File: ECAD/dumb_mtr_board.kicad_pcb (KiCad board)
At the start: 4 copper layers, 74.9 x 59.7 mm, 55 parts, among them J1 +5/24V, J2 UART, Q1 SOT-23-3, SW1 REV_BTN, SW2 FWD_BTN, U1 TPS62933DRLR, U2 TMC2209_SILENTSTEPSTICK, U3 LMC555xM

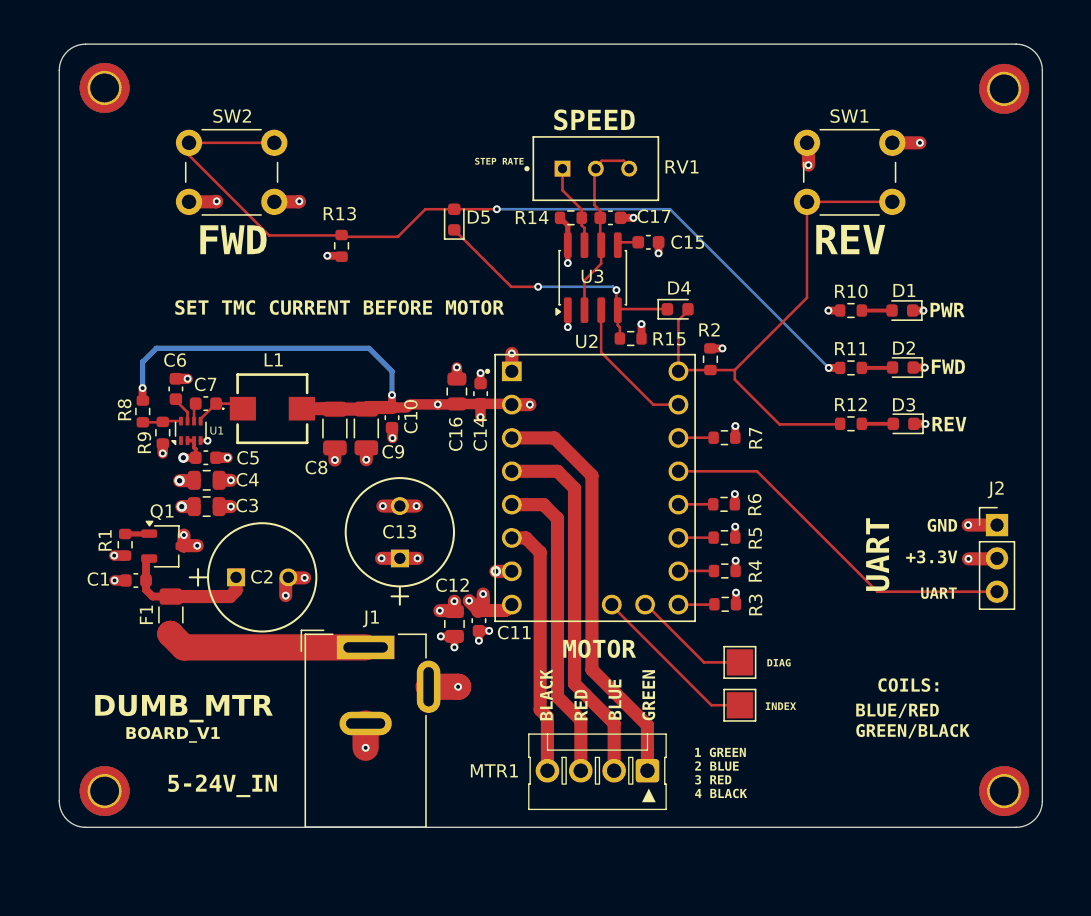
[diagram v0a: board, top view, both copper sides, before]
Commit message: Added stitching vias
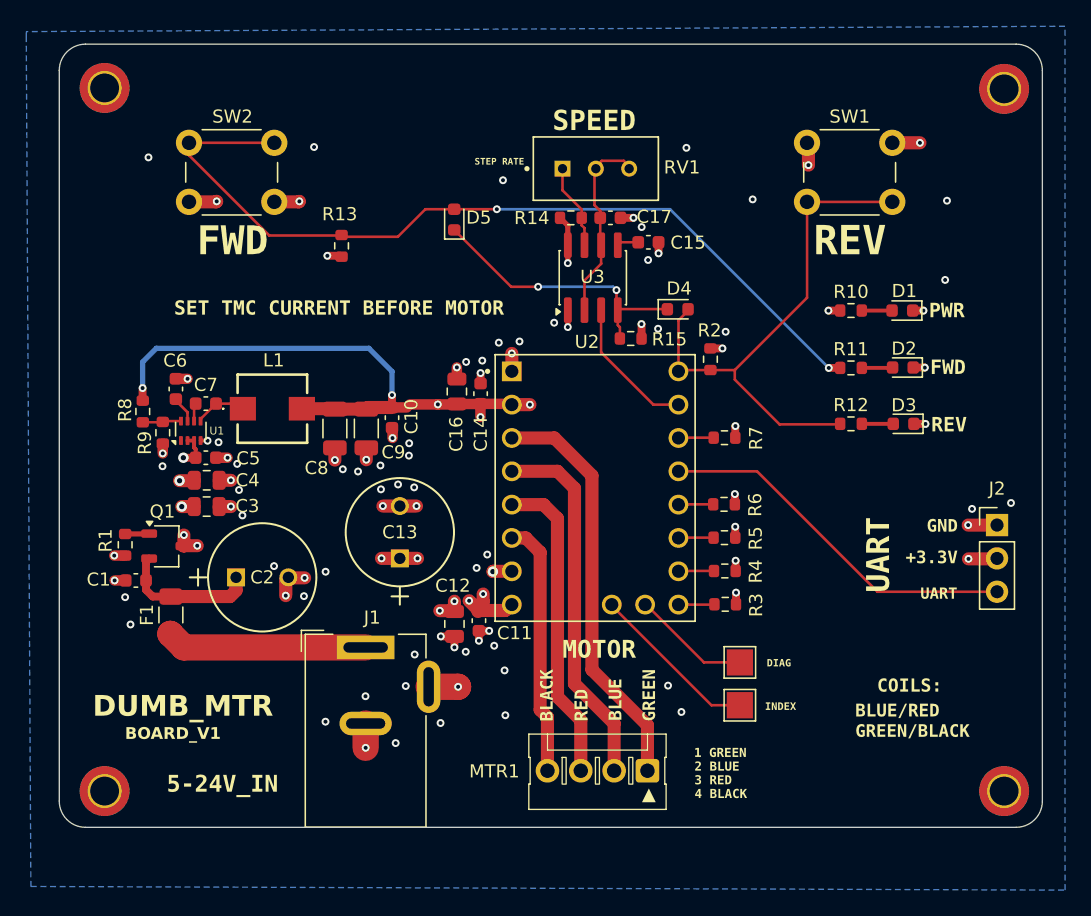
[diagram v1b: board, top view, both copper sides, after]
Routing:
- net GND: track 40.5 -> 40.7 mm, vias 39 -> 89
- added copper zone on B.Cu, net GND
